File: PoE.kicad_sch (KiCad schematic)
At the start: 78 parts, among them J13 Conn_01x03_Male, Q2 BSZ440N10NS3GATMA1, T1 PA2467NL, U24 TCMT1107

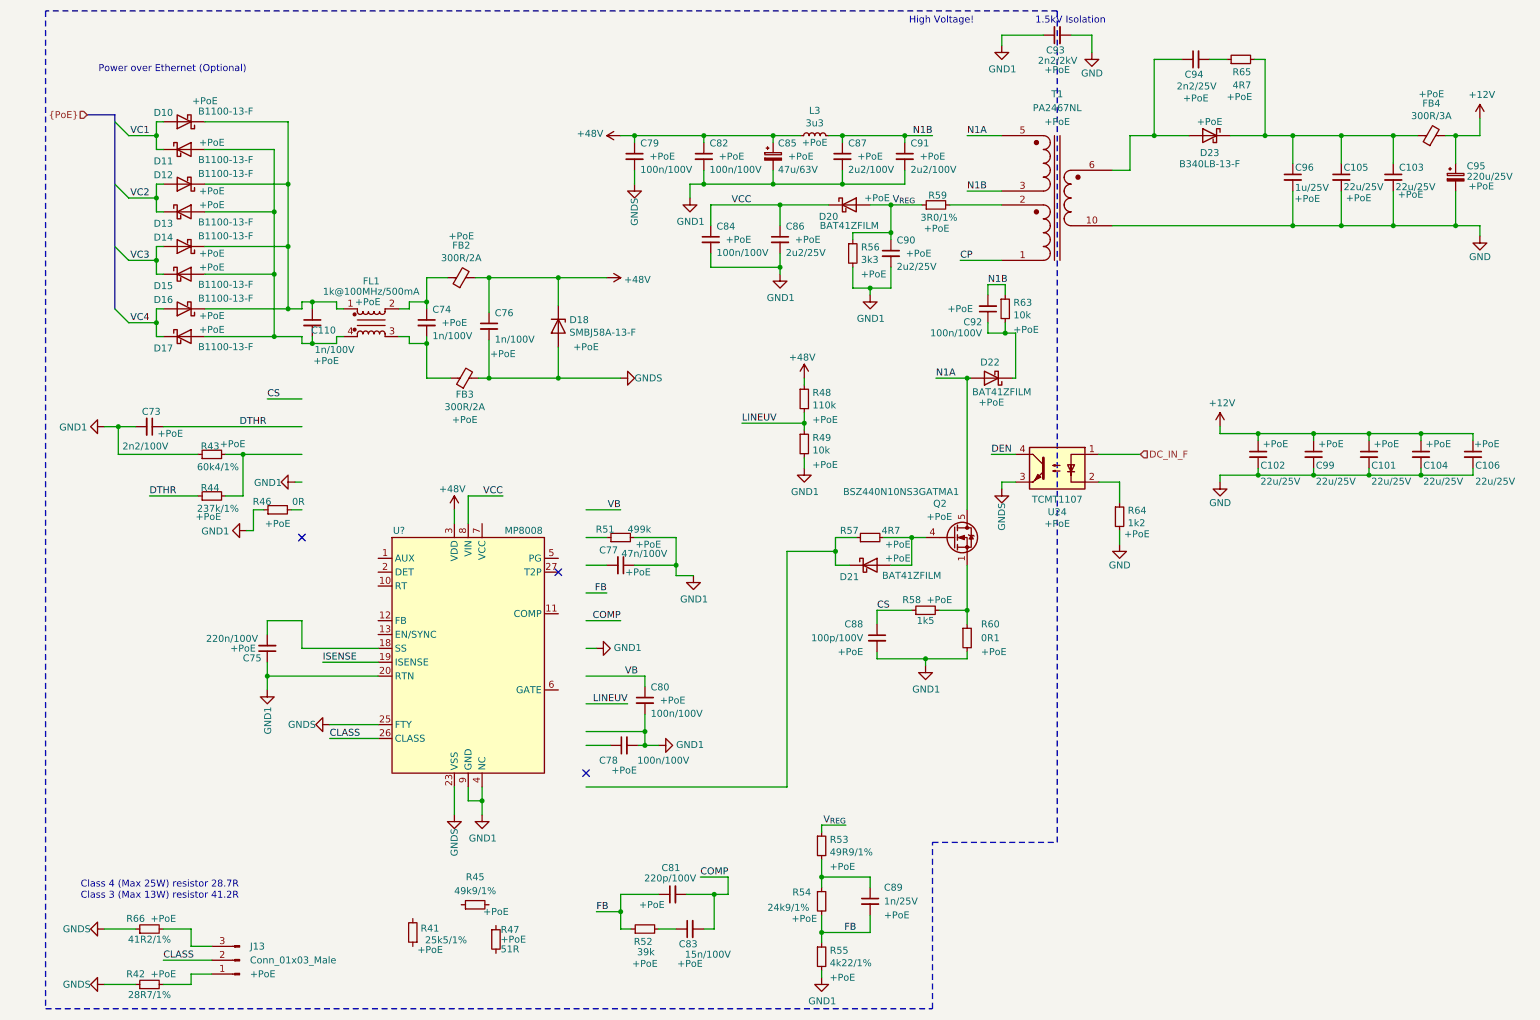
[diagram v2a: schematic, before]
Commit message: Rework PoE to use MP8008
Signed-off-by: Dominik Sliwa <dominik@sliwa.io>
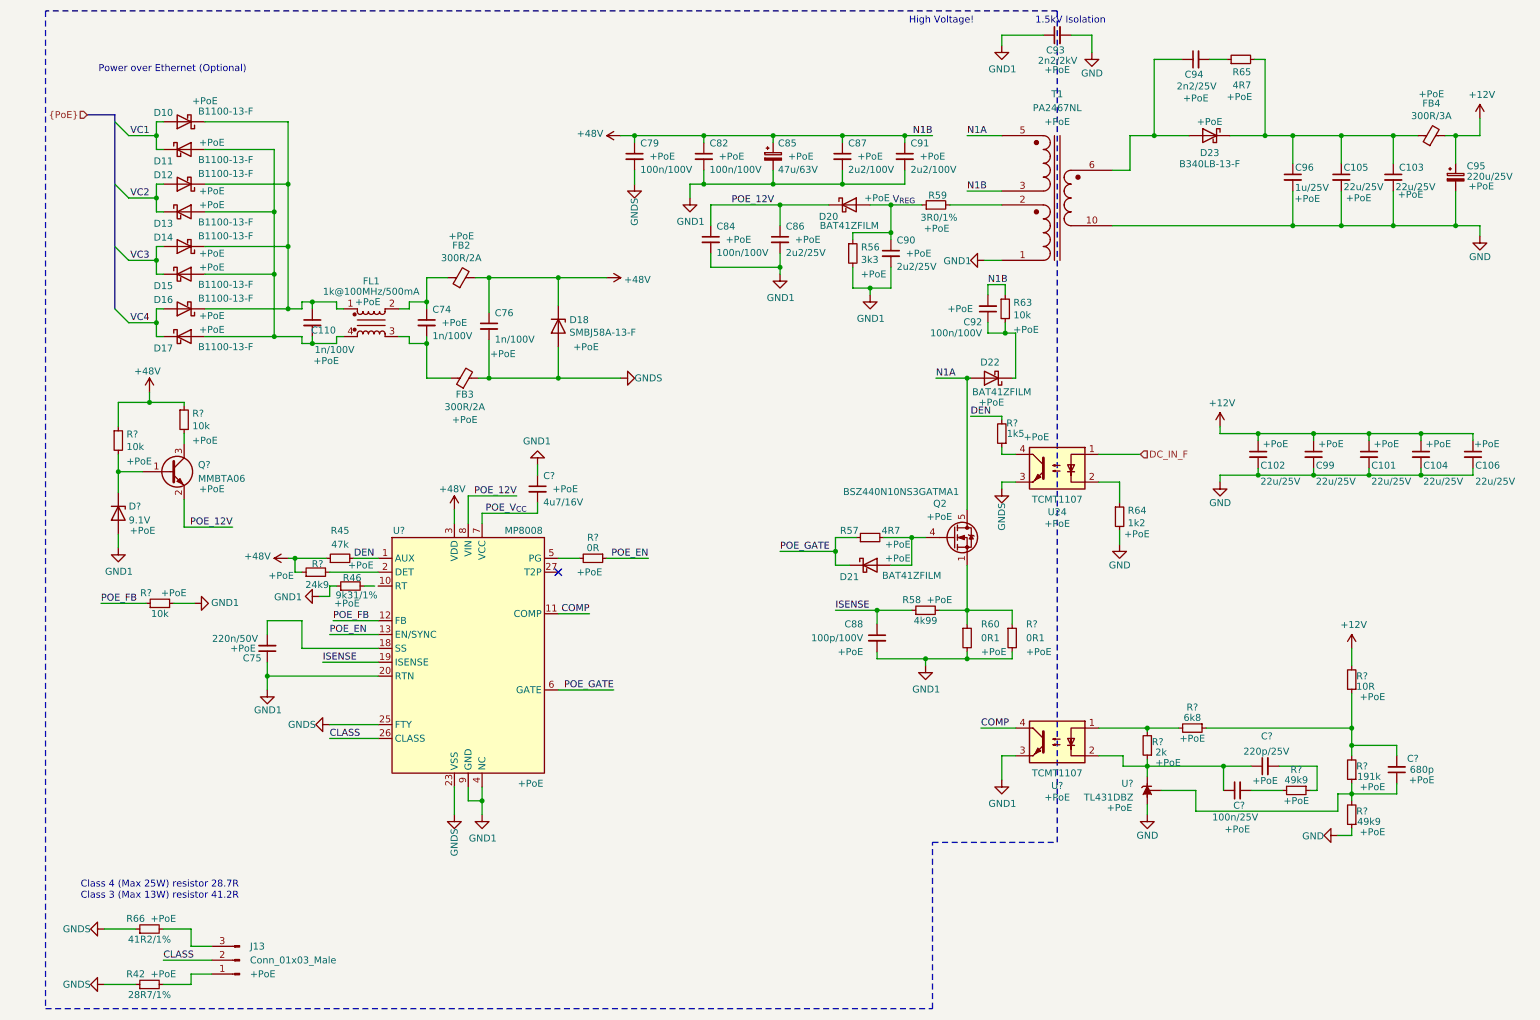
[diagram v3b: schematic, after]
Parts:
- removed C73: 2n2/100V, Capacitor_SMD:C_0805_2012Metric, symbol Device:C_Small
- removed C77: 47n/100V, Capacitor_SMD:C_0805_2012Metric, symbol Device:C_Small
- removed C78, C80: 100n/100V, Capacitor_SMD:C_0805_2012Metric, symbol Device:C_Small
- removed C81: 220p/100V, Capacitor_SMD:C_0805_2012Metric, symbol Device:C_Small
- removed C83: 15n/100V, Capacitor_SMD:C_0805_2012Metric, symbol Device:C_Small
- removed C89: 1n/25V, Capacitor_SMD:C_0402_1005Metric, symbol Device:C_Small
- removed L3: 3u3, Inductor_SMD:L_Taiyo-Yuden_NR-80xx, symbol Device:L_Small
- removed R41: 25k5/1%, Resistor_SMD:R_0402_1005Metric, symbol Device:R_Small
- removed R43: 60k4/1%, Resistor_SMD:R_0402_1005Metric, symbol Device:R_Small
- removed R44: 237k/1%, Resistor_SMD:R_0402_1005Metric, symbol Device:R_Small
- removed R47: 51R, Resistor_SMD:R_0805_2012Metric, symbol Device:R_Small
- removed R48: 110k, Resistor_SMD:R_0402_1005Metric, symbol Device:R_Small
- removed R49: 10k, Resistor_SMD:R_0402_1005Metric, symbol Device:R_Small
- removed R51: 499k, Resistor_SMD:R_0402_1005Metric, symbol Device:R_Small
- removed R52: 39k, Resistor_SMD:R_0402_1005Metric, symbol Device:R_Small
- removed R53: 49R9/1%, Resistor_SMD:R_0402_1005Metric, symbol Device:R_Small
- removed R54: 24k9/1%, Resistor_SMD:R_0402_1005Metric, symbol Device:R_Small
- removed R55: 4k22/1%, Resistor_SMD:R_0402_1005Metric, symbol Device:R_Small
- added C?: 680p, Capacitor_SMD:C_0402_1005Metric, symbol Device:C_Small
- added C?: 4u7/16V, Capacitor_SMD:C_0805_2012Metric, symbol Device:C_Small
- added C?: 100n/25V, Capacitor_SMD:C_0402_1005Metric, symbol Device:C_Small
- added C?: 220p/25V, Capacitor_SMD:C_0402_1005Metric, symbol Device:C_Small
- added D?: 9.1V, symbol Device:D_Zener
- added Q?: MMBTA06, Package_TO_SOT_SMD:SOT-23, symbol Transistor_BJT:MMBTA42
- added R? (x2): 49k9, Resistor_SMD:R_0402_1005Metric, symbol Device:R_Small
- added R?: 191k, Resistor_SMD:R_0402_1005Metric, symbol Device:R_Small
- added R?: 1k5, Resistor_SMD:R_0402_1005Metric, symbol Device:R_Small
- added R?: 10R, Resistor_SMD:R_0402_1005Metric, symbol Device:R_Small
- added R?: 0R1, Resistor_SMD:R_0805_2012Metric, symbol Device:R_Small
- added R?: 2k, Resistor_SMD:R_0402_1005Metric, symbol Device:R_Small
- added R? (x3): 10k, Resistor_SMD:R_0402_1005Metric, symbol Device:R_Small
- added R?: 24k9, Resistor_SMD:R_0402_1005Metric, symbol Device:R_Small
- added R?: 6k8, Resistor_SMD:R_0402_1005Metric, symbol Device:R_Small
- added R?: 0R, Resistor_SMD:R_0402_1005Metric, symbol Device:R_Small
- added U?: TL431DBZ, Package_TO_SOT_SMD:SOT-23, symbol Reference_Voltage:TL431DBZ
- added U?: TCMT1107, Package_SO:SOP-4_4.4x2.6mm_P1.27mm, symbol Isolator:TCMT1107
- C75: value 220n/100V -> 220n/50V
- R45: value 49k9/1% -> 47k
- R46: value 0R -> 9k31/1%
- R58: value 1k5 -> 4k99
- U?: Config (none) -> +PoE
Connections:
- net CP is gone; now on net GND1: T1.1 (N4B)
- net CS is gone; now on net ISENSE: C88.1, R58.1
- net N1B is gone; now on net +48V: C87.1, C91.1, C92.2, R63.1, T1.3 (N1B)
- net +12V: now also R?.2
- net +48V: now also R45.1, R?.1, R?.1, R?.1
- net COMP: now also U?.11 (COMP), U?.4
- net DEN: now also R45.2, U?.1 (AUX), R?.2; no longer U24.4
- net GND: now also R?.1, U?.3 (A)
- net GND1: now also C?.1, D?.2 (A), R?.2, R?.2, U?.3
- net at Q2.1 (S), Q2.2 (S), Q2.3 (S)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: now also R?.1
- net POE_GATE: now reaches D21.1 (K), R57.1
- net POE_GATE: now also U?.6 (GATE)
- net POE_FB: now reaches U?.12 (FB)
- net POE_FB: now also R?.1
- net POE_EN: now reaches U?.13 (EN/SYNC)
- net POE_EN: now also R?.1
- net at U?.2 (DET): now also R?.2
- net at U?.5 (PG): now also R?.2
- net POE_V_{CC}: now reaches U?.7 (VCC)
- net POE_V_{CC}: now also C?.2
- net VCC renamed POE_12V
- net POE_12V: now also Q?.2 (E)
- new net: C?.2, R?.1
- new net: C?.2, R?.2
- new net: C?.1, R?.1, R?.2, U?.2 (REF)
- new net: C?.2, R?.1, R?.1, R?.2
- new net: D?.1 (K), Q?.1 (B), R?.2
- new net: Q?.3 (C), R?.2
- new net: C?.1, C?.1, R?.1, U?.1 (K), U?.2
- new net: R?.1, U24.4
- new net: R?.2, R?.2, U?.1
- no-connect marks 3 -> 1
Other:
- moved on the sheet: R45, R46

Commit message: Assign Manufacturer/PartNumbers and align parts to 1.27mm grid
Signed-off-by: Stefan Agner <stefan@agner.ch>
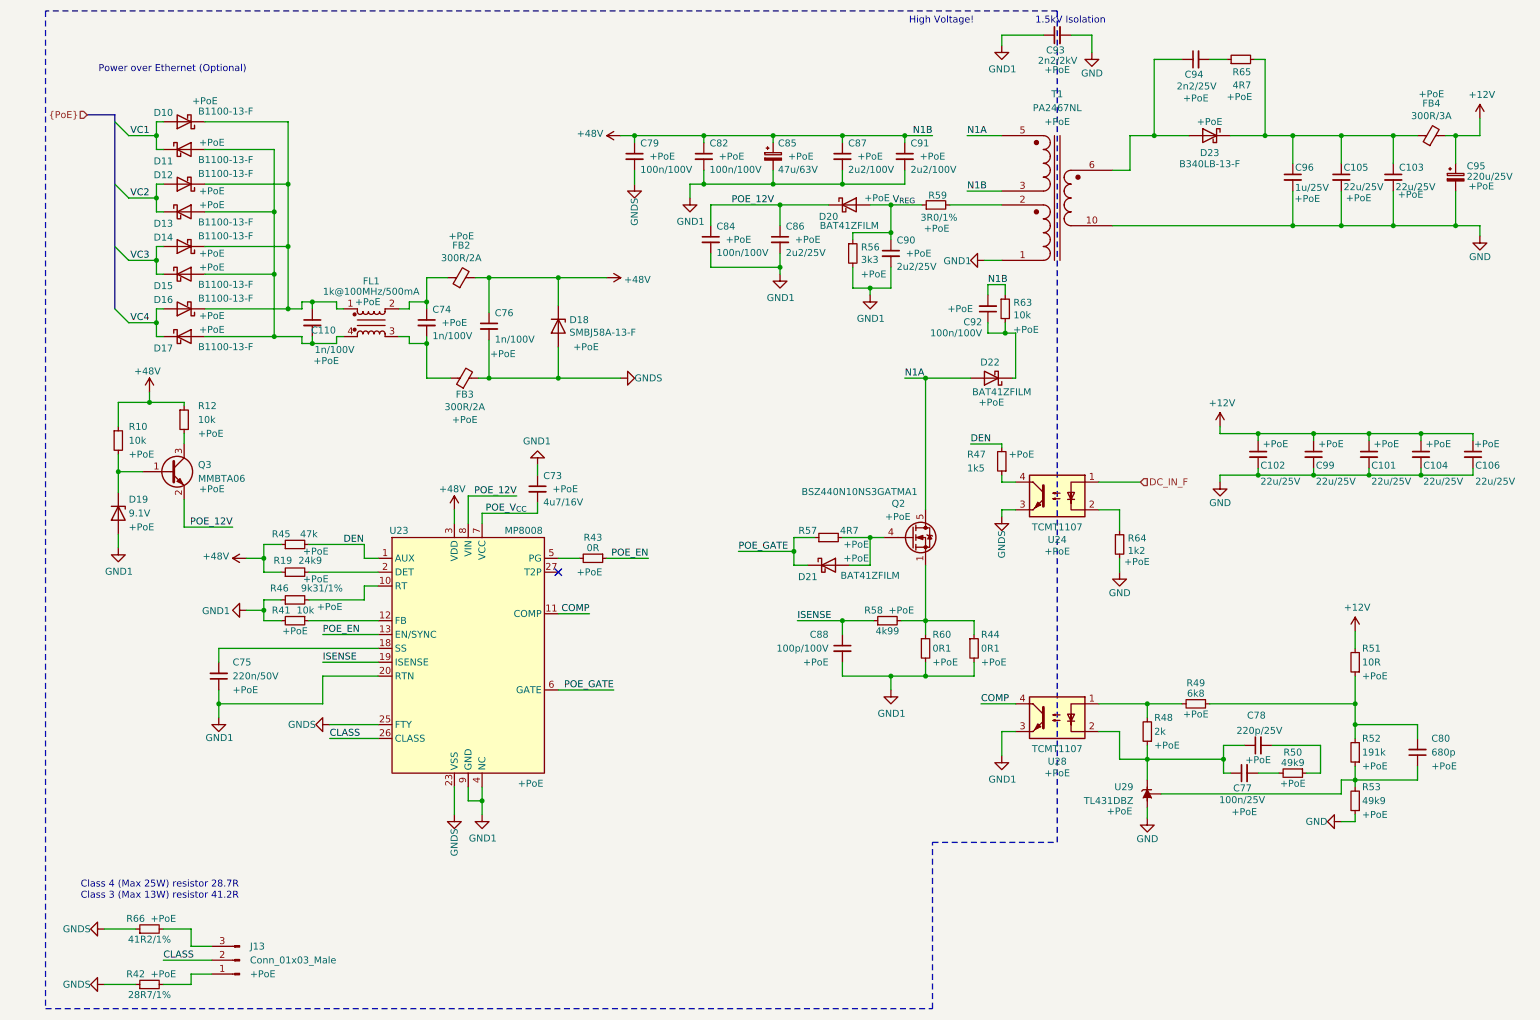
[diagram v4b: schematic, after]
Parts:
- D19: renamed from D?; footprint (none) -> Diode_SMD:D_SOD-123; Manufacturer (none) -> Diodes Incorporated; PartNumber (none) -> BZT52C9V1-7-F
- Q3: renamed from Q?; Manufacturer (none) -> Diodes Incorporated; PartNumber (none) -> MMBTA06-7-F
- U23: renamed from U?; Manufacturer (none) -> Monolithic Power Systems; PartNumber (none) -> MP8008GV-Z
- U29: renamed from U?; Manufacturer (none) -> Texas Instruments; PartNumber (none) -> TL431LIBCDBZR
- gave numbers to parts that had none: 18
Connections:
- net at R46.2: now also U23.10 (RT)
- net POE_FB: no longer names the net of R41.1, U23.12 (FB)
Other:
- moved on the sheet: C75, C77, C78, C80, C88, D21, Q2, R19, R41, R44, R45, R46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

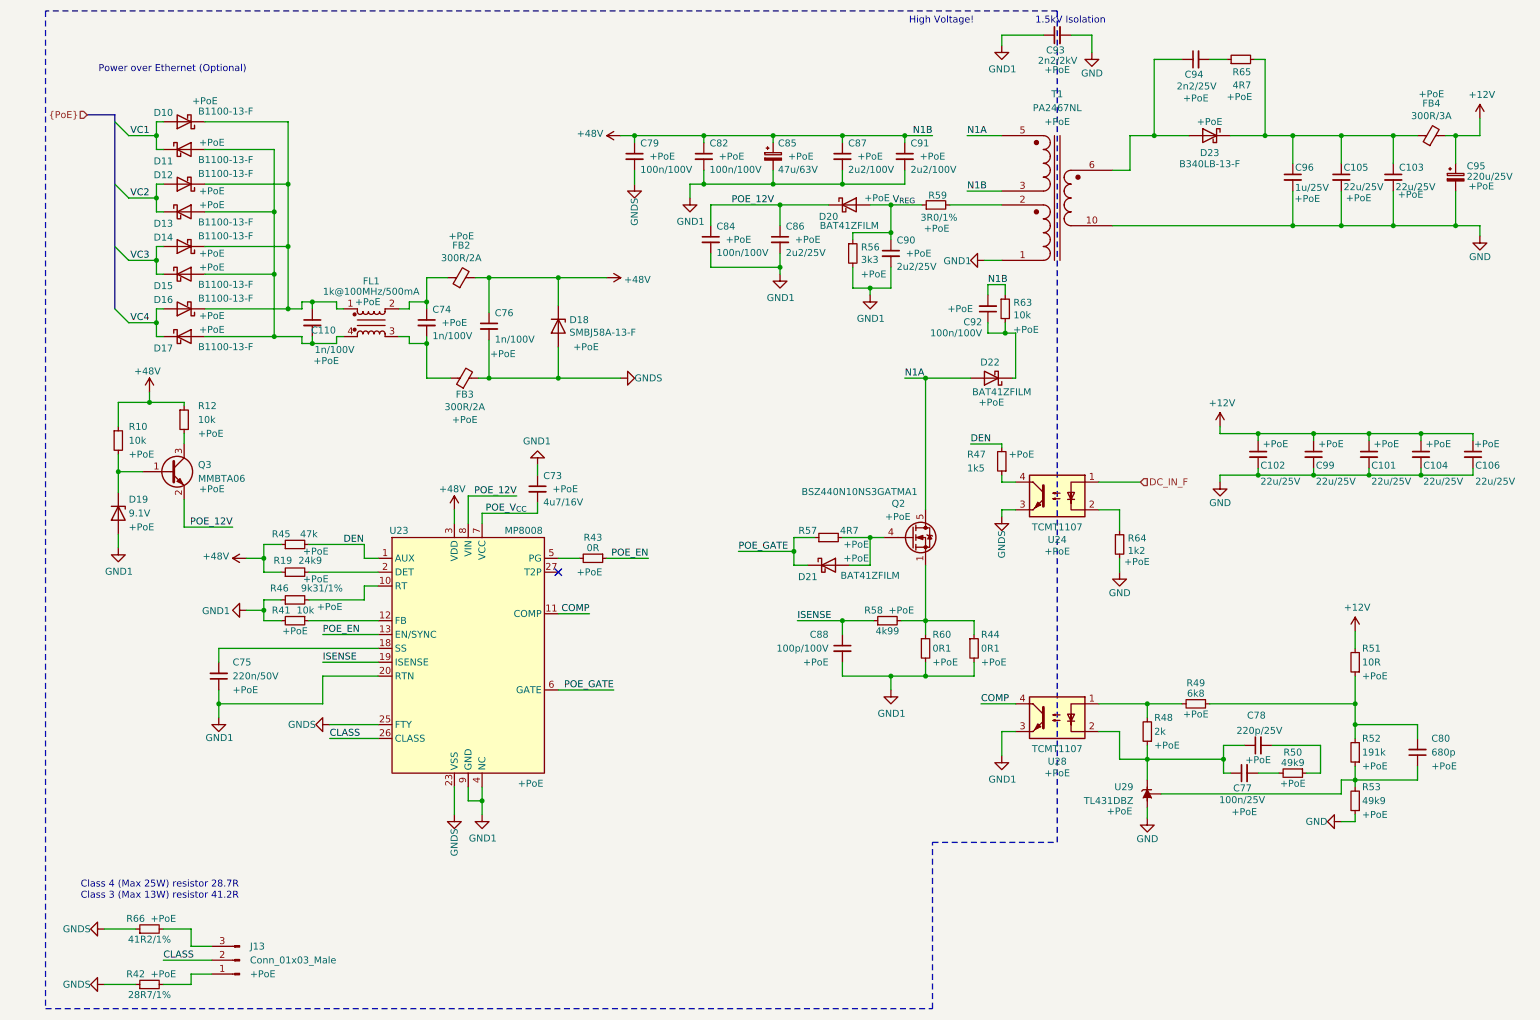
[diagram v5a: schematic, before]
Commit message: Yellow Proto1
Changes:
-name changed to yellow
-moved to 24-pin CP2102N
-routing

Signed-off-by: Dominik Sliwa <dominik@sliwa.io>
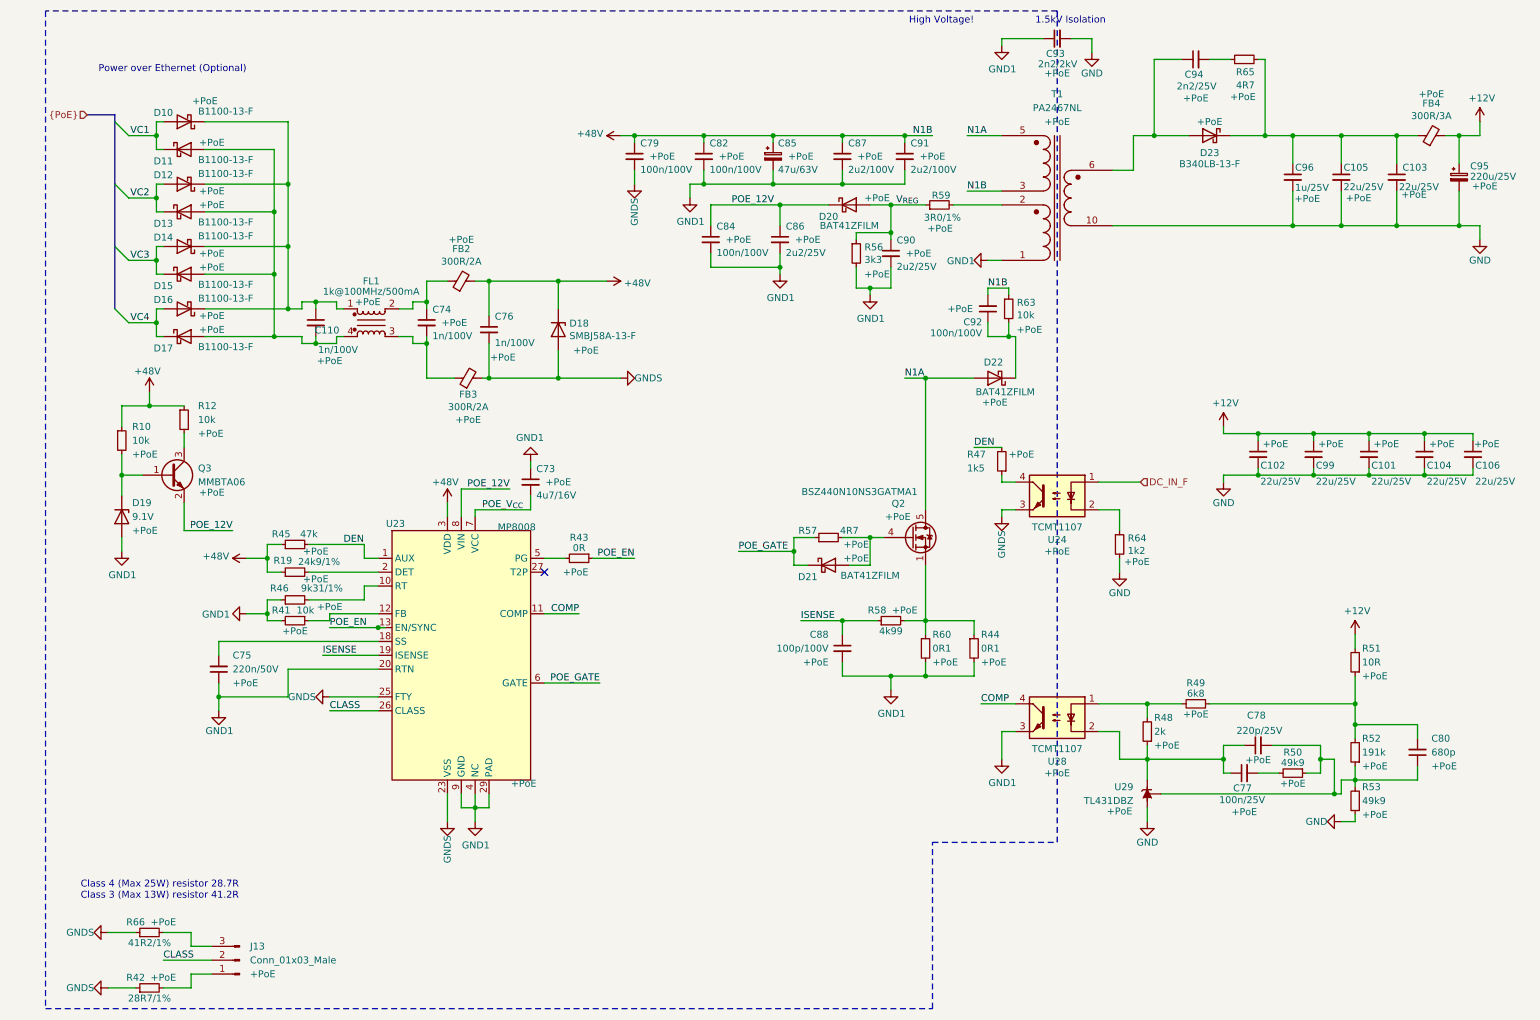
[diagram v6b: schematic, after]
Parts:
- C85: footprint Capacitor_SMD:C_Elec_8x10.2 -> Capacitor_SMD:C_Elec_10x10.2
- R19: value 24k9 -> 24k9/1%
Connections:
- net GND1: now also U23.29 (PAD)
- net at C78.2, R50.1: now also C80.1, R52.1, R53.2, U29.2 (REF)
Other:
- moved on the sheet: C103, C104, C110, C73, C75, C76, C93, C95, D18, D19, D22, FB2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
